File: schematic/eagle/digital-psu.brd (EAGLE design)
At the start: 101.3 x 77.5 mm, 79 parts, among them IC1 TL072P, IC2 TLC272P, Q1 MPSA56-TO92, T3 2N3055, T4 2N3055, T5 2N3055, T6 2N3704, X1 Vout, X2 PASS_TRANSISTORS, X3 AC_IN

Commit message: routing board 85% from completion
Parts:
- removed T6: 2N3704, transistor:TO92
- added T1: (no value), transistor:TO92-EBC
- moved JP1 26.9 mm to (40.6, 73.7), turned to 180 degrees
- moved JP2 22.5 mm to (39.4, 54.6), turned to 0 degrees
- moved C11 5.08 mm to (61.0, 41.9), turned to 270 degrees
- moved C16 5.08 mm to (63.5, 71.1)
- moved D11 4.58 mm to (85.1, 61.0)
- moved S2 2.84 mm to (44.5, 48.3)
- moved C15 2.54 mm to (55.9, 47.0), turned to 180 degrees
- moved D9 2.54 mm to (68.6, 34.3)
- moved S1 2.54 mm to (27.9, 48.3)
- moved C9 1.80 mm to (64.8, 52.1), turned to 0 degrees
- moved JP3 1.42 mm to (29.2, 55.2)
- moved D12 1.27 mm to (92.7, 57.1)
- moved D10 1.27 mm to (58.4, 57.1)
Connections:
- removed net N$10 (its old number): R29.1, R30.1, T6.1
- removed net N$18 (its old number): D10.A, IC2.3
- removed net N$21: C10.1, C9.1, C9.2, IC2.1, IC2.2, R14.2, R15.1, R20.2, T6.2
- removed net N$22 (its old number): R25.1, R26.1-1, R26.2-1
- new net ADJ_VOLT: D10.A, IC2.3, R25.1, R26.1-1, R26.2-1
- new net N$17: R29.1, R30.1, T1.B
- new net N$31: C9.2, IC2.1, R15.1, T1.C
- new net N$38: C10.1, C9.1, IC2.2, R14.2, R20.2
- net GND: now also T1.E; no longer T6.3
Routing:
- net N$17: track 0.00 -> 171.9 mm, vias 0 -> 3
- net VCC: track 151.5 -> 312.4 mm, vias 0 -> 5
- net N$41: track 0.00 -> 128.6 mm, vias 0 -> 2
- net GND_HIGHER: track 67.1 -> 168.0 mm, vias 0 -> 2
- net N$2: track 0.00 -> 93.6 mm, vias 0 -> 2
- net N$4: track 0.00 -> 58.7 mm, vias 0 -> 1
- net N$38: track 0.00 -> 50.4 mm, vias 0 -> 2
- net VNEG: track 19.4 -> 64.5 mm, vias 0 -> 3
- net N$28: track 0.00 -> 42.8 mm, vias 0 -> 2
- net N$34: track 0.00 -> 42.7 mm, vias 0 -> 2
- net VZENER: track 13.3 -> 43.1 mm, vias 0 -> 2
- net N$29: track 0.00 -> 28.8 mm, vias 0 -> 2
- net N$33: track 0.00 -> 24.1 mm
- net N$31: track 0.00 -> 18.9 mm, vias 0 -> 2
- net ADJ_VOLT: track 0.00 -> 18.4 mm, vias 0 -> 1
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
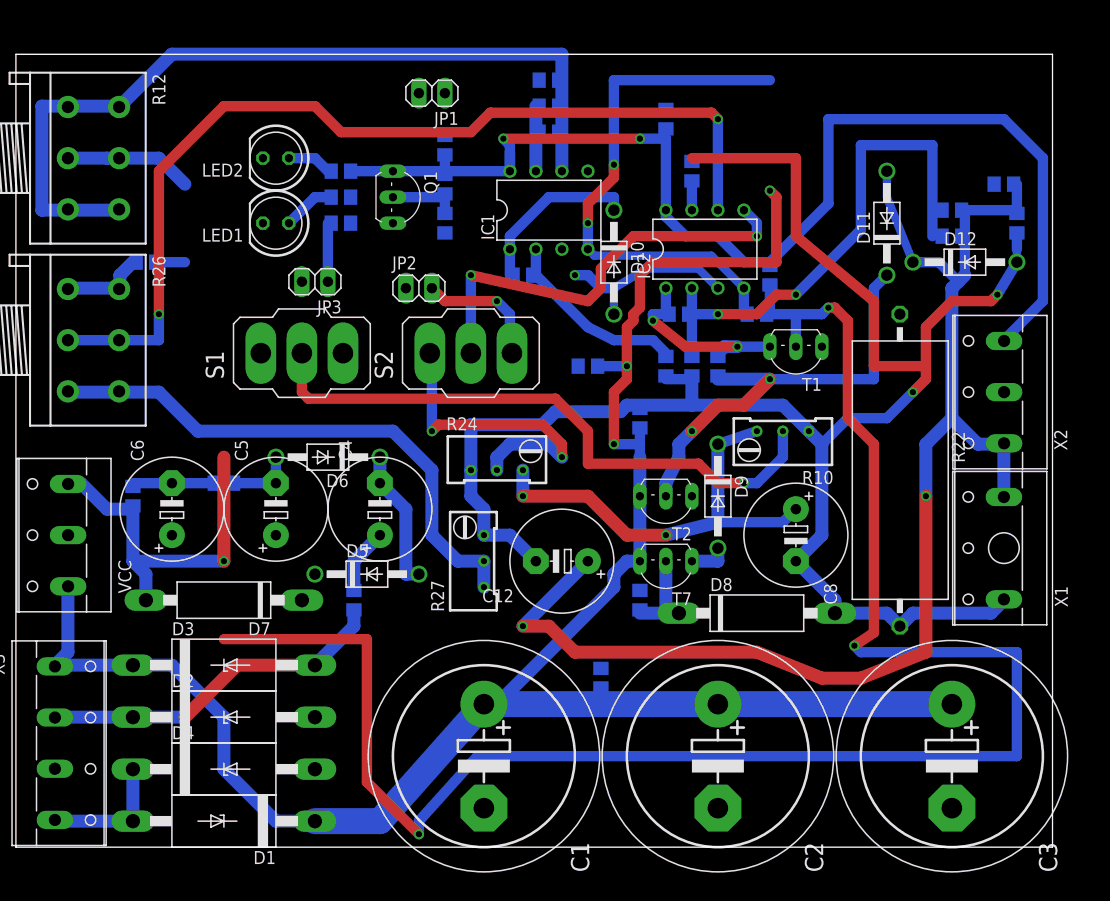
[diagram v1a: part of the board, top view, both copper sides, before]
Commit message: finished routing board
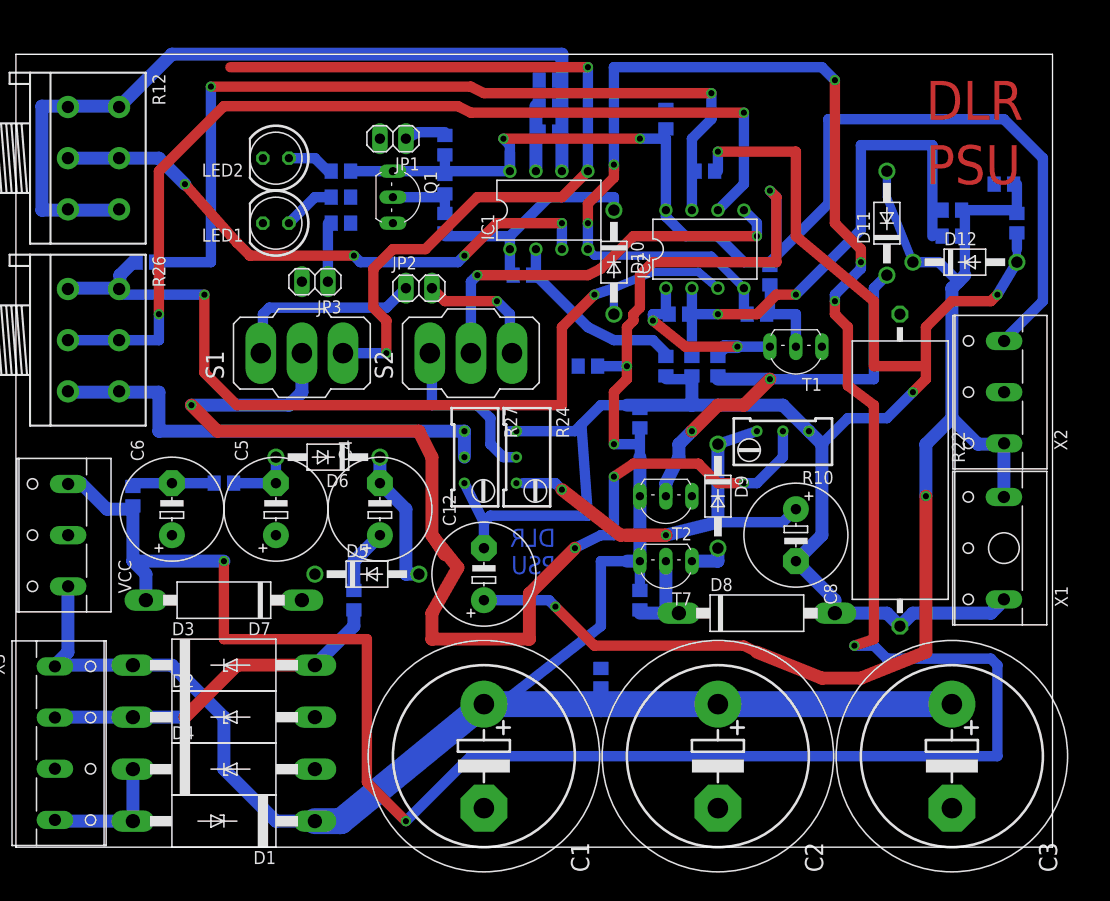
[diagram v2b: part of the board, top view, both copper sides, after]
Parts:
- moved R27 10.2 mm to (45.1, 38.1), turned to 180 degrees
- moved C12 7.73 mm to (45.7, 26.7), turned to 90 degrees
- moved JP1 5.85 mm to (36.8, 69.2)
- moved R24 3.17 mm to (50.2, 38.1), turned to 180 degrees
- moved C14 1.27 mm to (67.3, 66.0), turned to 180 degrees
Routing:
- net VNEG: track 64.5 -> 272.2 mm, vias 3 -> 8
- net N$17: track 171.9 -> 7.62 mm, vias 3 -> 0
- net N$44: track 0.00 -> 83.2 mm, vias 0 -> 2
- net N$30: track 2.54 -> 83.5 mm, vias 0 -> 2
- net ADJ_VOLT: track 18.4 -> 79.8 mm, vias 1 -> 2
- net N$4: track 58.7 -> 114.2 mm, vias 1 -> 4
- net ADJ_CURR: track 12.5 -> 56.8 mm, vias 0 -> 4
- net N$33: track 24.1 -> 0.00 mm
- net N$43: track 0.00 -> 18.8 mm
- net N$29: track 28.8 -> 16.3 mm, vias 2 -> 0
- net N$36: track 53.7 -> 45.1 mm
- net N$15: track 16.8 -> 23.2 mm
- net GND_HIGHER: track 168.0 -> 173.1 mm, vias 2 -> 3
- net N$41: track 128.6 -> 124.4 mm
- net GND: track 0.00 -> 3.96 mm
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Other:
- board text added: "DLR PSU"

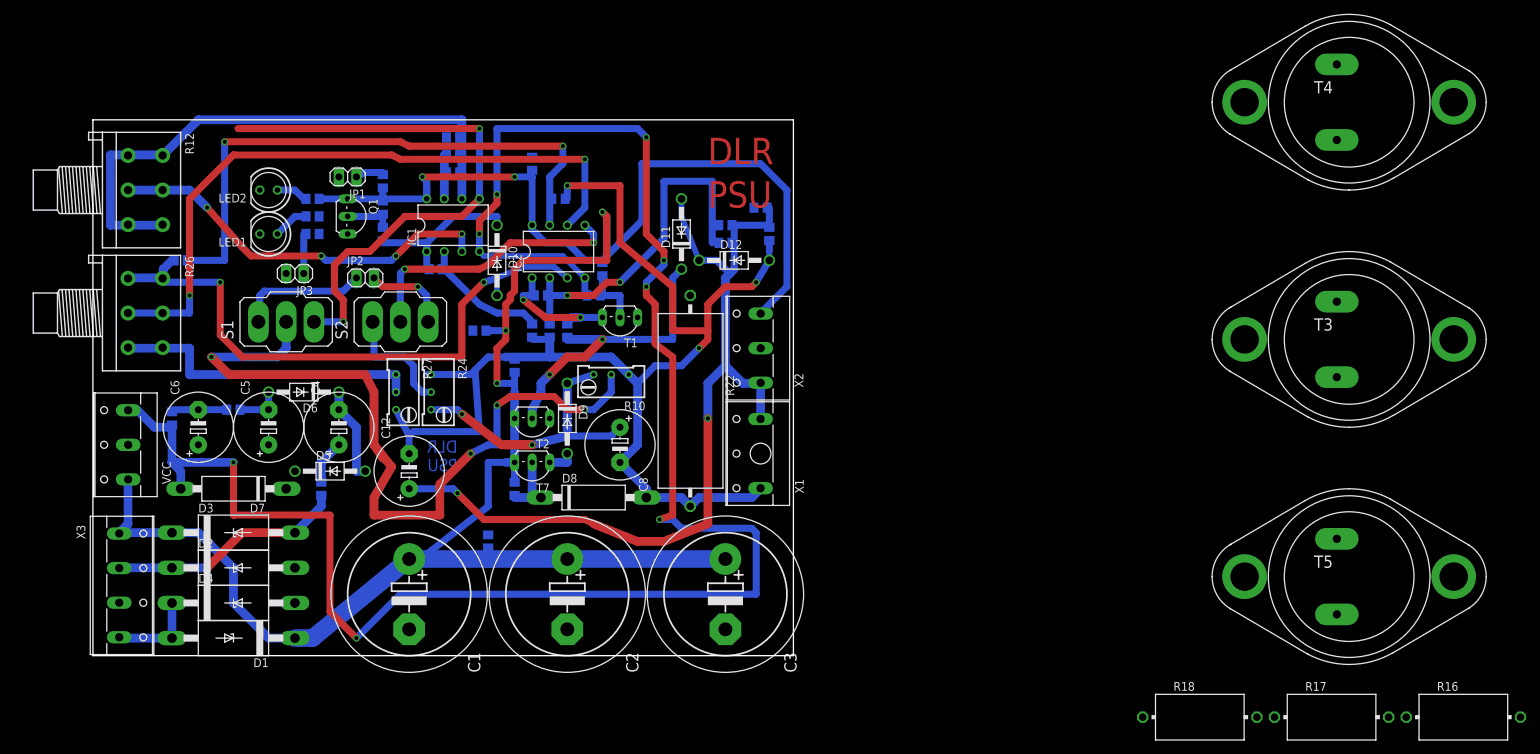
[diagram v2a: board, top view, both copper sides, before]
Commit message: adjusted spacing between traces, added ground plane bottom and copper polygon on top
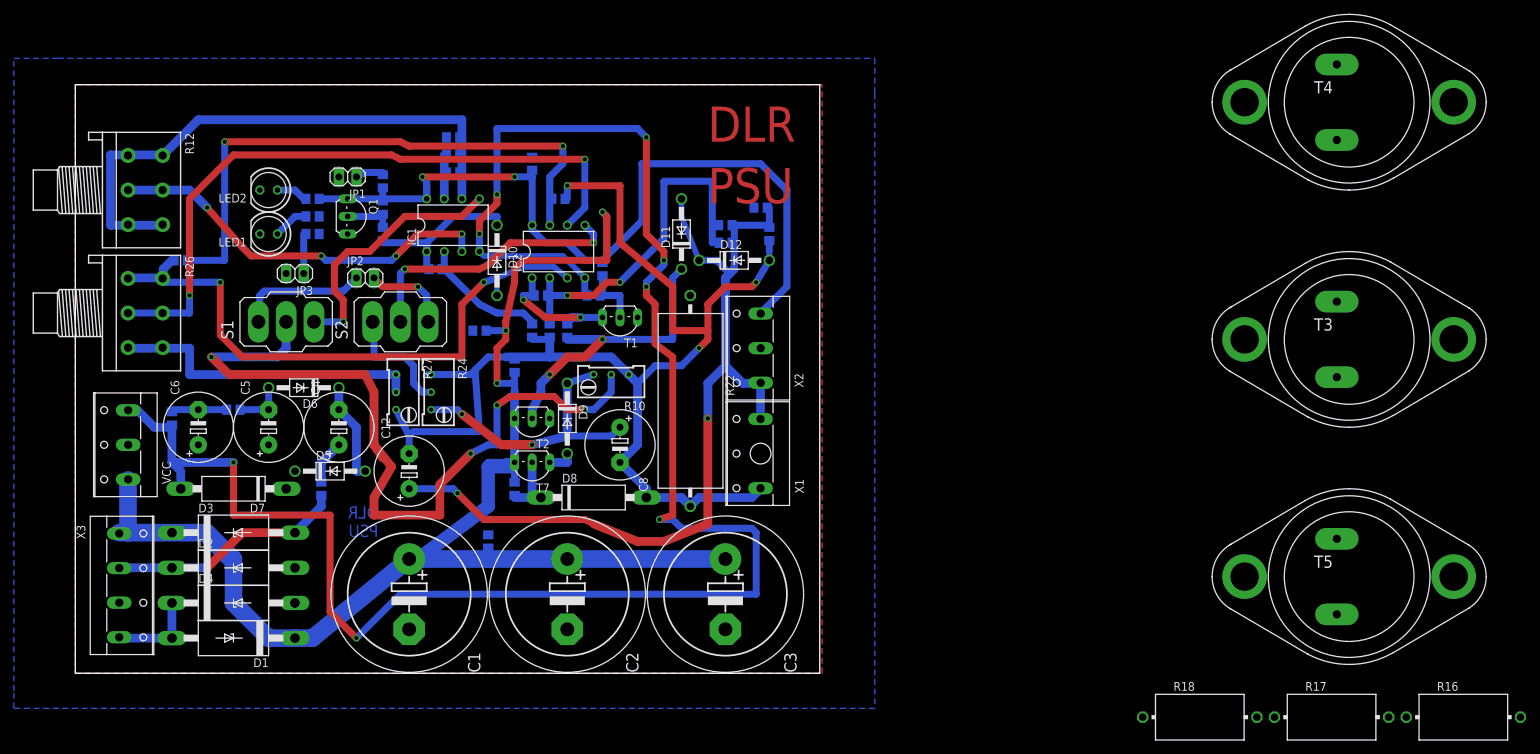
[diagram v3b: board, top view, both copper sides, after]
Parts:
- moved D6 0.63 mm to (30.5, 38.7)
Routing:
- net VCC: track 316.2 -> 362.5 mm
- net N$44: track 83.2 -> 38.1 mm, vias 2 -> 1
- net N$7: track 6.35 -> 6.98 mm
- net N$6: track 13.8 -> 14.4 mm
- added copper zone on layer 16, net GND
- added copper zone on layer 1, net N$13
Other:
- board size 101.3 x 77.5 mm -> 107.6 x 85.1 mm

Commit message: created gerber files
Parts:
- moved R16 84.2 mm to (115.6, 7.62)
- moved R18 81.7 mm to (115.6, 59.7)
- moved R17 76.8 mm to (115.6, 34.3)
- moved T4 51.2 mm to (130.8, 73.7)
- moved T5 50.3 mm to (132.1, 20.3)
- moved T3 49.5 mm to (132.1, 47.0)
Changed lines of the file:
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@@
 <layer number="15" name="Route15" color="4" fill="6" visible="no" active="no"/>
 <layer number="16" name="Bottom" color="1" fill="1" visible="yes" active="yes"/>
-<layer number="17" name="Pads" color="2" fill="1" visible="no" active="yes"/>
-<layer number="18" name="Vias" color="2" fill="1" visible="no" active="yes"/>
-<layer number="19" name="Unrouted" color="6" fill="1" visible="no" active="yes"/>
-<layer number="20" name="Dimension" color="15" fill="1" visible="no" active="yes"/>
-<layer number="21" name="tPlace" color="7" fill="1" visible="no" active="yes"/>
-<layer number="22" name="bPlace" color="7" fill="1" visible="no" active="yes"/>
-<layer number="23" name="tOrigins" color="15" fill="1" visible="no" active="yes"/>
-<layer number="24" name="bOrigins" color="15" fill="1" visible="no" active="yes"/>
-<layer number="25" name="tNames" color="7" fill="1" visible="no" active="yes"/>
-<layer number="26" name="bNames" color="7" fill="1" visible="no" active="yes"/>
-<layer number="27" name="tValues" color="7" fill="1" visible="no" active="yes"/>
-<layer number="28" name="bValues" color="7" fill="1" visible="no" active="yes"/>
-<layer number="29" name="tStop" color="7" fill="3" visible="no" active="yes"/>
-<layer number="30" name="bStop" color="7" fill="6" visible="no" active="yes"/>
-<layer number="31" name="tCream" color="7" fill="4" visible="no" active="yes"/>
-<layer number="32" name="bCream" color="7" fill="5" visible="no" active="yes"/>
-<layer number="33" name="tFinish" color="6" fill="3" visible="no" active="yes"/>
-<layer number="34" name="bFinish" color="6" fill="6" visible="no" active="yes"/>
-<layer number="35" name="tGlue" color="7" fill="4" visible="no" active="yes"/>
-<layer number="36" name="bGlue" color="7" fill="5" visible="no" active="yes"/>
-<layer number="37" name="tTest" color="7" fill="1" visible="no" active="yes"/>
-<layer number="38" name="bTest" color="7" fill="1" visible="no" active="yes"/>
-<layer number="39" name="tKeepout" color="4" fill="11" visible="no" active="yes"/>
-<layer number="40" name="bKeepout" color="1" fill="11" visible="no" active="yes"/>
-<layer number="41" name="tRestrict" color="4" fill="10" visible="no" active="yes"/>
-<layer number="42" name="bRestrict" color="1" fill="10" visible="no" active="yes"/>
-<layer number="43" name="vRestrict" color="2" fill="10" visible="no" active="yes"/>
-<layer number="44" name="Drills" color="7" fill="1" visible="no" active="yes"/>
-<layer number="45" name="Holes" color="7" fill="1" visible="no" active="yes"/>
-<layer number="46" name="Milling" color="3" fill="1" visible="no" active="yes"/>
-<layer number="47" name="Measures" color="7" fill="1" visible="no" active="yes"/>
-<layer number="48" name="Document" color="7" fill="1" visible="no" active="yes"/>
-<layer number="49" name="Reference" color="7" fill="1" visible="no" active="yes"/>
-<layer number="51" name="tDocu" color="7" fill="1" visible="no" active="yes"/>
-<layer number="52" name="bDocu" color="7" fill="1" visible="no" active="yes"/>
+<layer number="17" name="Pads" color="2" fill="1" visible="yes" active="yes"/>
+<layer number="18" name="Vias" color="2" fill="1" visible="yes" active="yes"/>
+<layer number="19" name="Unrouted" color="6" fill="1" visible="yes" active="yes"/>
+<layer number="20" name="Dimension" color="15" fill="1" visible="yes" active="yes"/>
+<layer number="21" name="tPlace" color="7" fill="1" visible="yes" active="yes"/>
+<layer number="22" name="bPlace" color="7" fill="1" visible="yes" active="yes"/>
+<layer number="23" name="tOrigins" color="15" fill="1" visible="yes" active="yes"/>
+<layer number="24" name="bOrigins" color="15" fill="1" visible="yes" active="yes"/>
+<layer number="25" name="tNames" color="7" fill="1" visible="yes" active="yes"/>
+<layer number="26" name="bNames" color="7" fill="1" visible="yes" active="yes"/>
+<layer number="27" name="tValues" color="7" fill="1" visible="yes" active="yes"/>
+<layer number="28" name="bValues" color="7" fill="1" visible="yes" active="yes"/>
+<layer number="29" name="tStop" color="7" fill="3" visible="yes" active="yes"/>
+<layer number="30" name="bStop" color="7" fill="6" visible="yes" active="yes"/>
+<layer number="31" name="tCream" color="7" fill="4" visible="yes" active="yes"/>
+<layer number="32" name="bCream" color="7" fill="5" visible="yes" active="yes"/>
+<layer number="33" name="tFinish" color="6" fill="3" visible="yes" active="yes"/>
+<layer number="34" name="bFinish" color="6" fill="6" visible="yes" active="yes"/>
+<layer number="35" name="tGlue" color="7" fill="4" visible="yes" active="yes"/>
+<layer number="36" name="bGlue" color="7" fill="5" visible="yes" active="yes"/>
+<layer number="37" name="tTest" color="7" fill="1" visible="yes" active="yes"/>
+<layer number="38" name="bTest" color="7" fill="1" visible="yes" active="yes"/>
+<layer number="39" name="tKeepout" color="4" fill="11" visible="yes" active="yes"/>
+<layer number="40" name="bKeepout" color="1" fill="11" visible="yes" active="yes"/>
+<layer number="41" name="tRestrict" color="4" fill="10" visible="yes" active="yes"/>
+<layer number="42" name="bRestrict" color="1" fill="10" visible="yes" active="yes"/>
+<layer number="43" name="vRestrict" color="2" fill="10" visible="yes" active="yes"/>
+<layer number="44" name="Drills" color="7" fill="1" visible="yes" active="yes"/>
+<layer number="45" name="Holes" color="7" fill="1" visible="yes" active="yes"/>
+<layer number="46" name="Milling" color="3" fill="1" visible="yes" active="yes"/>
+<layer number="47" name="Measures" color="7" fill="1" visible="yes" active="yes"/>
+<layer number="48" name="Document" color="7" fill="1" visible="yes" active="yes"/>
+<layer number="49" name="Reference" color="7" fill="1" visible="yes" active="yes"/>
+<layer number="51" name="tDocu" color="7" fill="1" visible="yes" active="yes"/>
+<layer number="52" name="bDocu" color="7" fill="1" visible="yes" active="yes"/>
 <layer number="90" name="Modules" color="5" fill="1" visible="no" active="no"/>
 <layer number="91" name="Nets" color="2" fill="1" visible="no" active="no"/>
@@
 <attribute name="SPICEPREFIX" value="R" x="68.58" y="46.99" size="1.778" layer="28" rot="MR270" display="off"/>
 </element>
-<element name="R16" library="rcl" package="VTA55" value="0.1" x="198.12" y="-8.89"/>
-<element name="R17" library="rcl" package="VTA55" value="0.1" x="179.07" y="-8.89"/>
-<element name="R18" library="rcl" package="VTA55" value="0.1" x="160.02" y="-8.89"/>
+<element name="R16" library="rcl" package="VTA55" value="0.1" x="115.57" y="7.62"/>
+<element name="R17" library="rcl" package="VTA55" value="0.1" x="115.57" y="34.29"/>
+<element name="R18" library="rcl" package="VTA55" value="0.1" x="115.57" y="59.69"/>
 <element name="R19" library="eagle-ltspice" package="R0805" value="1k" x="96.52" y="64.77" rot="MR0">
 <attribute name="SPICEMODEL" value="NONE" x="96.52" y="64.77" size="1.778" layer="28" rot="MR0" display="off"/>
@@
 <element name="S1" library="switch" package="320-916" value="EXTERNAL_VOLT_CTRL" x="27.94" y="48.26" rot="R90"/>
 <element name="S2" library="switch" package="320-916" value="EXT_CURR_CTRL" x="44.45" y="48.26" rot="R90"/>
-<element name="T3" library="transistor" package="TO3" value="2N3055" x="181.61" y="45.72"/>
-<element name="T4" library="transistor" package="TO3" value="2N3055" x="181.61" y="80.01"/>
-<element name="T5" library="transistor" package="TO3" value="2N3055" x="181.61" y="11.43"/>
+<element name="T3" library="transistor" package="TO3" value="2N3055" x="132.08" y="46.99"/>
+<element name="T4" library="transistor" package="TO3" value="2N3055" x="130.81" y="73.66"/>
+<element name="T5" library="transistor" package="TO3" value="2N3055" x="132.08" y="20.32"/>
 <element name="X1" library="con-wago-500" package="W237-113" value="Vout" x="95.25" y="29.21" rot="R90">
 <attribute name="OC_FARNELL" value="unknown" x="95.25" y="29.21" size="1.778" layer="27" rot="R90" display="off"/>
@@
 <contactref element="T3" pad="E"/>
 <contactref element="R18" pad="1"/>
-<wire x1="151.765" y1="-8.89" x2="179.832" y2="40.259" width="0" layer="19" extent="1-1"/>
+<wire x1="107.315" y1="59.69" x2="130.302" y2="41.529" width="0" layer="19" extent="1-1"/>
 </signal>
 <signal name="N$25" airwireshidden="yes">
 <contactref element="T4" pad="E"/>
 <contactref element="R17" pad="1"/>
-<wire x1="170.815" y1="-8.89" x2="179.832" y2="74.549" width="0" layer="19" extent="1-1"/>
+<wire x1="107.315" y1="34.29" x2="129.032" y2="68.199" width="0" layer="19" extent="1-1"/>
 </signal>
 <signal name="N$26" airwireshidden="yes">
 <contactref element="T5" pad="E"/>
 <contactref element="R16" pad="1"/>
-<wire x1="189.865" y1="-8.89" x2="179.832" y2="5.969" width="0" layer="19" extent="1-1"/>
+<wire x1="107.315" y1="7.62" x2="130.302" y2="14.859" width="0" layer="19" extent="1-1"/>
 </signal>
 <signal name="N$27" airwireshidden="yes">
@@
 <contactref element="X2" pad="2"/>
 <contactref element="T2" pad="E"/>
-<wire x1="179.832" y1="16.891" x2="179.832" y2="51.181" width="0" layer="19" extent="1-1"/>
-<wire x1="179.832" y1="85.471" x2="179.832" y2="51.181" width="0" layer="19" extent="1-1"/>
-<wire x1="96.54" y1="44.45" x2="179.832" y2="51.181" width="0" layer="19" extent="1-1"/>
+<wire x1="130.302" y1="25.781" x2="130.302" y2="52.451" width="0" layer="19" extent="1-1"/>
+<wire x1="129.032" y1="79.121" x2="130.302" y2="52.451" width="0" layer="19" extent="1-1"/>
+<wire x1="96.54" y1="44.45" x2="130.302" y2="52.451" width="0" layer="19" extent="1-1"/>
 <wire x1="95.57" y1="64.77" x2="96.54" y2="44.45" width="0" layer="19" extent="16-16"/>
 <wire x1="66.04" y1="34.29" x2="96.54" y2="44.45" width="0" layer="19" extent="1-1"/>
